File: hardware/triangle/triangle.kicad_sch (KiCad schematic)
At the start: 63 parts, among them J1 USB_C_Receptacle_USB2.0_16P, J2 USB_C_Receptacle_USB2.0_16P

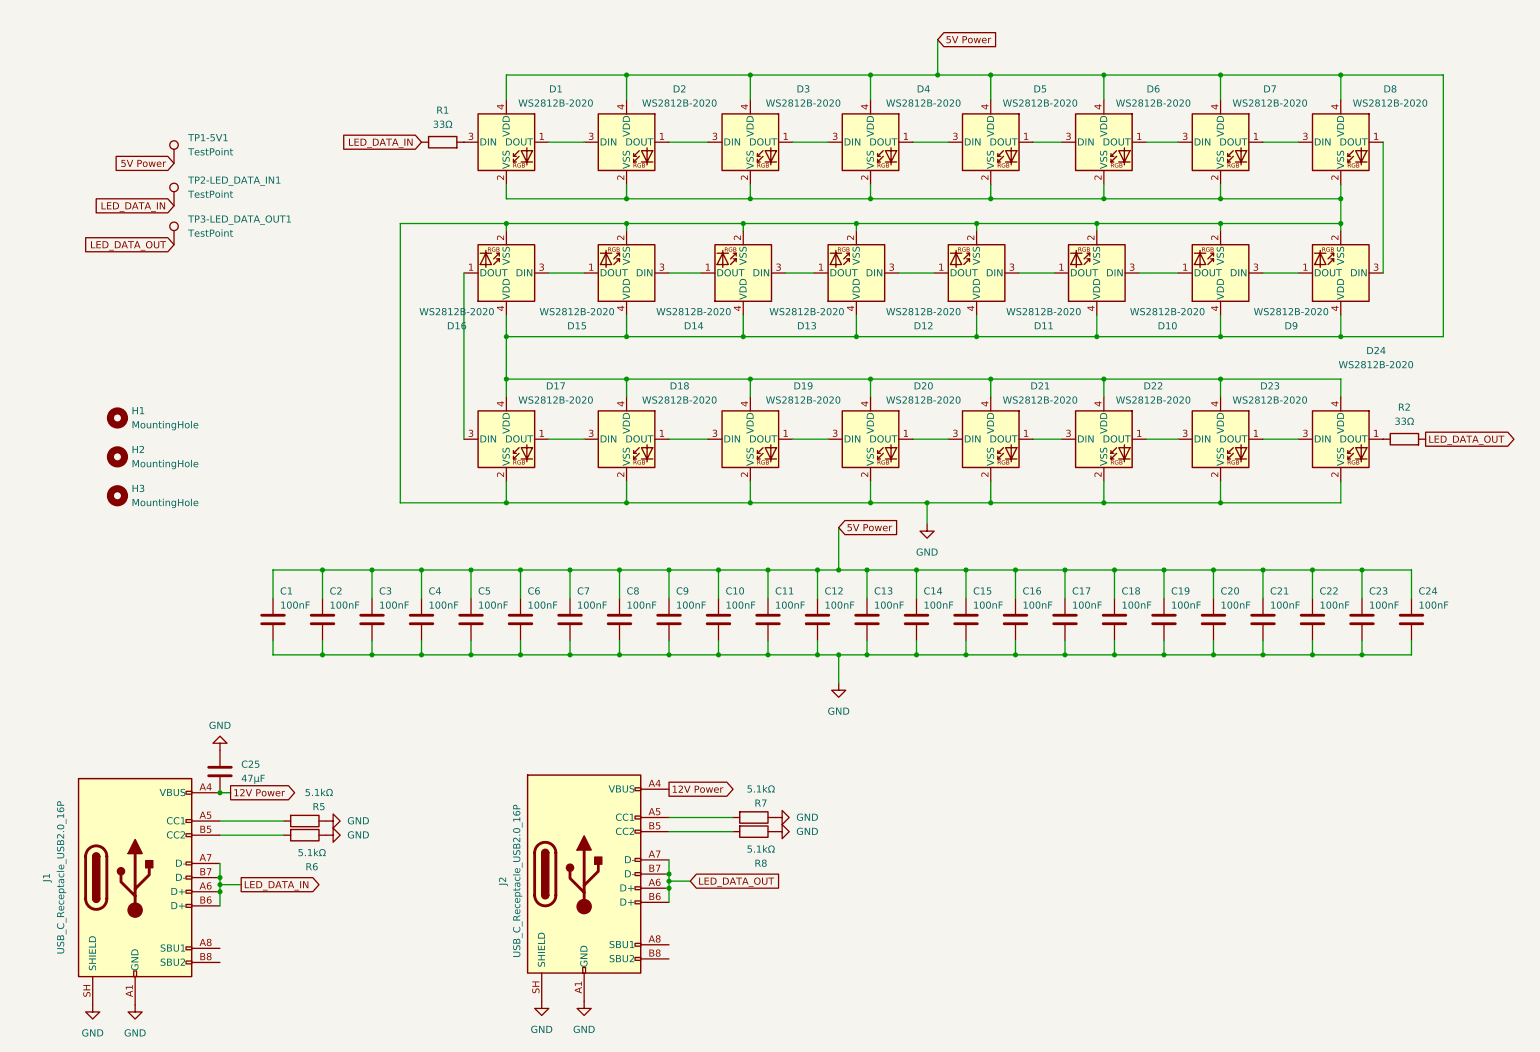
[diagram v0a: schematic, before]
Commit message: add more power items
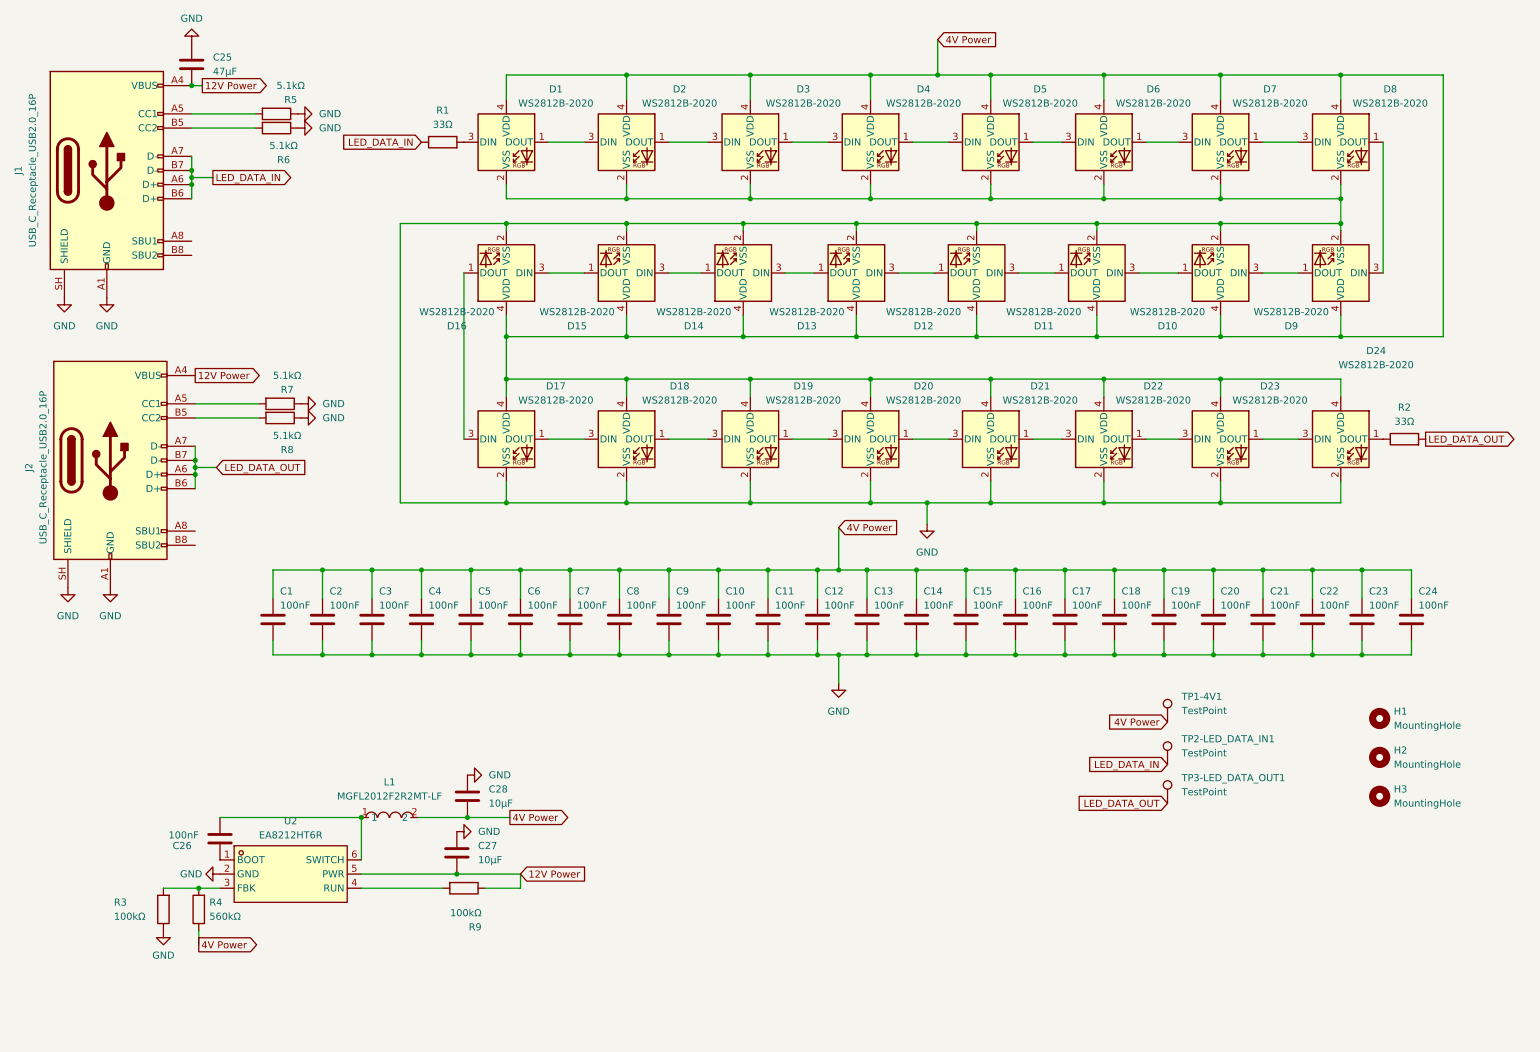
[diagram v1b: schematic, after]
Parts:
- added C26: 100nF, Capacitor_SMD:C_0402_1005Metric, symbol Device:C
- added C27, C28: 10µF, Capacitor_SMD:C_0603_1608Metric, symbol Device:C
- added L1: MGFL2012F2R2MT-LF, footprints:L0805, symbol easyeda2kicad:MGFL2012F2R2MT-LF
- added R3, R9: 100kΩ, Resistor_SMD:R_0402_1005Metric, symbol Device:R
- added R4: 560kΩ, Resistor_SMD:R_0402_1005Metric, symbol Device:R
- added U2: EA8212HT6R, footprints:SOT-23-6_L2.9-W1.6-P0.95-LS2.8-BR, symbol new:EA8212HT6R
- renumbered TP1-5V1 to TP1-4V1
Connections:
- net 12V Power: now also C27.1, R9.1, U2.5 (PWR)
- net GND: now also C27.2, C28.2, R3.1, U2.2 (GND)
- net 5V Power renamed 4V Power
- net 4V Power: now also C28.1, L1.2, R4.1
- new net: R3.2, R4.2, U2.3 (FBK)
- new net: R9.2, U2.4 (RUN)
- new net: C26.1, U2.1 (BOOT)
- new net: C26.2, L1.1, U2.6 (SWITCH)
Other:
- moved on the sheet: C25, H1, H2, H3, J1, J2, R5, R6, R7, R8, TP1-4V1, TP2-LED_DATA_IN1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

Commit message: fixing schematic
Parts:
- removed C25: 47µF, Capacitor_SMD:C_1206_3216Metric, symbol Device:C
- removed C26: 100nF, Capacitor_SMD:C_0402_1005Metric, symbol Device:C
- removed C27, C28: 10µF, Capacitor_SMD:C_0603_1608Metric, symbol Device:C
- removed J1, J2: USB_C_Receptacle_USB2.0_16P, footprints:TYPE-C-SMD_USB4120-03-C, symbol Connector:USB_C_Receptacle_USB2.0_16P
- removed L1: MGFL2012F2R2MT-LF, footprints:L0805, symbol easyeda2kicad:MGFL2012F2R2MT-LF
- removed R3, R9: 100kΩ, Resistor_SMD:R_0402_1005Metric, symbol Device:R
- removed R4: 560kΩ, Resistor_SMD:R_0402_1005Metric, symbol Device:R
- removed R5, R6, R7, R8: 5.1kΩ, Resistor_SMD:R_0603_1608Metric, symbol Device:R
- removed U2: EA8212HT6R, footprints:SOT-23-6_L2.9-W1.6-P0.95-LS2.8-BR, symbol new:EA8212HT6R
- R1, R2: symbol Device:R -> Device:R_US
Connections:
- net 4V Power renamed +4V
- net +4V: no longer TP1-4V1.1
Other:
- moved on the sheet: C1, C10, C11, C12, C13, C14, C15, C16, C17, C18, C19, C2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

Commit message: more moving things around
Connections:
- net +4V: now also TP1-4V1.1
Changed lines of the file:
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@@
 	(wire
 		(pts
-			(xy 50.165 159.385) (xy 45.085 159.385)
+			(xy 45.085 159.385) (xy 50.8 159.385)
 		)
 		(stroke

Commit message: fix part numbering
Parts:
- C1, C10, C11, C12, C13, C14, C15, C16, C17, C18, C19, C2, C20, C21, C22, C23, C24, C3, C4, C5, C6, C7, C8, C9: JLCPCB Part # C1525 -> (none); LCSC Part # (none) -> C1525
- D1, D10, D11, D12, D13, D14, D15, D16, D17, D18, D19, D2, D20, D21, D22, D23, D24, D3, D4, D5, D6, D7, D8, D9: LCSC Part # (none) -> C965555
- R1, R2: JLCPCB Part # C23140 -> (none); LCSC Part # (none) -> C23140
